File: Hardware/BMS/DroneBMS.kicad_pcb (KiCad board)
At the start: 4 copper layers, 90 x 51 mm, 42 parts, among them J1 BattLevel (ADC), J2 BattLevel (ADC), U1 LMR51430, U2 AMS1117-3.3

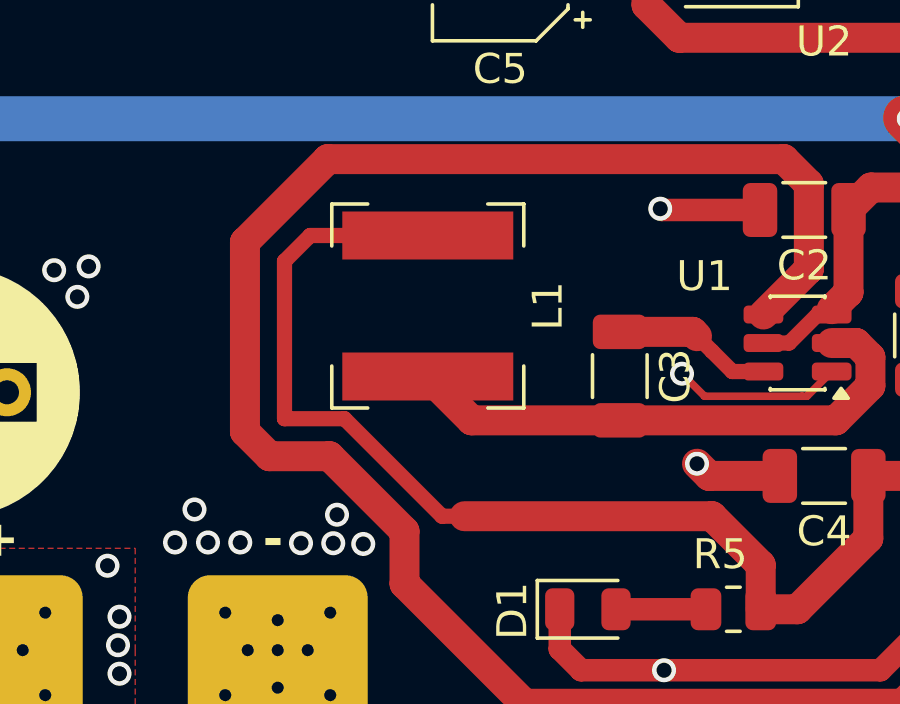
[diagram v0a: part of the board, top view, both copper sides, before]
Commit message: Updated Pcb Footprints
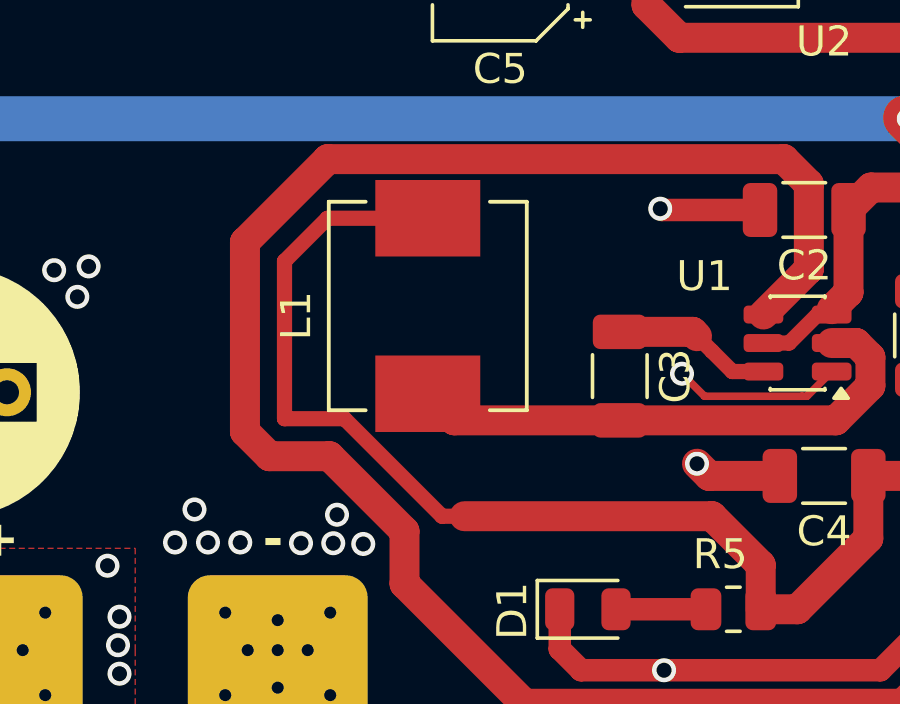
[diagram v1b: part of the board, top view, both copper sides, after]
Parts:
- L1: footprint Inductor_SMD:L_Bourns-SRN6028 -> Custom_Footprints:IND_VSAB0630-4R7M
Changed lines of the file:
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@@
 		)
 	)
-	(footprint "Inductor_SMD:L_Bourns-SRN6028"
+	(footprint "Custom_Footprints:IND_VSAB0630-4R7M"
 		(layer "F.Cu")
 		(at 160.5262 107.4928 90)
-		(descr "Bourns SRN6028 series SMD inductor")
-		(tags "Bourns SRN6028 SMD inductor")
 		(property "Reference" "L1"
-			(at 0 4 90)
+			(at -0.325 -4.385 90)
 			(layer "F.SilkS")
 			(effects
@@
 		)
 		(property "Value" "4.7uH"
-			(at 4.263 0.234 0)
+			(at 7.295 4.365 90)
 			(layer "F.Fab")
 			(effects
@@
 		(property "Datasheet" "~"
 			(at 0 0 90)
-			(unlocked yes)
 			(layer "F.Fab")
 			(hide yes)
@@
 		(property "Description" "Inductor"
 			(at 0 0 90)
-			(unlocked yes)
 			(layer "F.Fab")
 			(hide yes)
@@
 		(attr smd)
 		(fp_line
-			(start 3.4 -3.2)
-			(end 2 -3.2)
+			(start 3.475 -3.3)
+			(end 3.475 -2.07)
 			(stroke
-				(width 0.12)
+				(width 0.127)
 				(type solid)
 			)
@@
 		)
 		(fp_line
-			(start 3.4 -3.2)
-			(end 3.4 -2)
+			(start -3.475 -3.3)
+			(end 3.475 -3.3)
 			(stroke
-				(width 0.12)
+				(width 0.127)
 				(type solid)
 			)
@@
 		)
 		(fp_line
-			(start -3.4 -3.2)
-			(end -2 -3.2)
+			(start -3.475 -2.07)
+			(end -3.475 -3.3)
 			(stroke
-				(width 0.12)
+				(width 0.127)
 				(type solid)
 			)
@@
 		)
 		(fp_line
-			(start -3.4 -3.2)
-			(end -3.4 -2)
+			(start 3.475 2.07)
+			(end 3.475 3.3)
 			(stroke
-				(width 0.12)
+				(width 0.127)
 				(type solid)
 			)
@@
 		)
 		(fp_line
-			(start 3.4 3.2)
-			(end 3.4 2)
+			(start 3.475 3.3)
+			(end -3.475 3.3)
 			(stroke
-				(width 0.12)
+				(width 0.127)
 				(type solid)
 			)
@@
 		)
 		(fp_line
-			(start 3.4 3.2)
-			(end 2 3.2)
+			(start -3.475 3.3)
+			(end -3.475 2.07)
 			(stroke
-				(width 0.12)
+				(width 0.127)
 				(type solid)
 			)
@@
 		)
 		(fp_line
-			(start -3.4 3.2)
-			(end -3.4 2)
+			(start 3.725 -3.55)
+			(end 3.725 -2)
 			(stroke
-				(width 0.12)
+				(width 0.05)
 				(type solid)
 			)
-			(layer "F.SilkS")
+			(layer "F.CrtYd")
 		)
 		(fp_line
-			(start -3.4 3.2)
-			(end -2 3.2)
+			(start -3.725 -3.55)
+			(end 3.725 -3.55)
 			(stroke
-				(width 0.12)
+				(width 0.05)
 				(type solid)
 			)
-			(layer "F.SilkS")
+			(layer "F.CrtYd")
 		)
 		(fp_line
-			(start 3.3 -3.1)
-			(end 3.3 3.1)
+			(start 4.45 -2)
+			(end 4.45 2)
 			(stroke
 				(width 0.05)
@@
 		)
 		(fp_line
-			(start -3.3 -3.1)
-			(end 3.3 -3.1)
+			(start 3.725 -2)
+			(end 4.45 -2)
 			(stroke
 				(width 0.05)
@@
 		)
 		(fp_line
-			(start -3.3 -3.1)
-			(end -3.3 3.1)
+			(start -3.725 -2)
+			(end -3.725 -3.55)
 			(stroke
 				(width 0.05)
@@
 		)
 		(fp_line
-			(start 3.3 3.1)
-			(end -3.3 3.1)
+			(start -3.725 -2)
+			(end -4.45 -2)
 			(stroke
 				(width 0.05)
@@
 		)
 		(fp_line
-			(start 3.3 -3.1)
-			(end 3.3 3.1)
+			(start -4.45 -2)
+			(end -4.45 2)
 			(stroke
-				(width 0.1)
+				(width 0.05)
 				(type solid)
 			)
-			(layer "F.Fab")
+			(layer "F.CrtYd")
 		)
 		(fp_line
-			(start -3.3 -3.1)
-			(end 3.3 -3.1)
+			(start 4.45 2)
+			(end 3.725 2)
 			(stroke
-				(width 0.1)
+				(width 0.05)
 				(type solid)
 			)
-			(layer "F.Fab")
+			(layer "F.CrtYd")
 		)
 		(fp_line
-			(start -3.3 -3.1)
-			(end -3.3 3.1)
+			(start 3.725 2)
+			(end 3.725 3.55)
 			(stroke
-				(width 0.1)
+				(width 0.05)
+				(type solid)
+			)
+			(layer "F.CrtYd")
+		)
+		(fp_line
+			(start -4.45 2)
+			(end -3.725 2)
+			(stroke
+				(width 0.05)
+				(type solid)
+			)
+			(layer "F.CrtYd")
+		)
+		(fp_line
+			(start 3.725 3.55)
+			(end -3.725 3.55)
+			(stroke
+				(width 0.05)
+				(type solid)
+			)
+			(layer "F.CrtYd")
+		)
+		(fp_line
+			(start -3.725 3.55)
+			(end -3.725 2)
+			(stroke
+				(width 0.05)
+				(type solid)
+			)
+			(layer "F.CrtYd")
+		)
+		(fp_line
+			(start 3.475 -3.3)
+			(end 3.475 3.3)
+			(stroke
+				(width 0.127)
 				(type solid)
 			)
@@
 		)
 		(fp_line
-			(start 3.3 3.1)
-			(end -3.3 3.1)
+			(start -3.475 -3.3)
+			(end 3.475 -3.3)
 			(stroke
-				(width 0.1)
+				(width 0.127)
 				(type solid)
 			)
 			(layer "F.Fab")
 		)
-		(fp_text user "${REFERENCE}"
-			(at 0 0 90)
+		(fp_line
+			(start 3.475 3.3)
+			(end -3.475 3.3)
+			(stroke
+				(width 0.127)
+				(type solid)
+			)
 			(layer "F.Fab")
-			(effects
-				(font
-					(size 1 1)
-					(thickness 0.15)
-				)
+		)
+		(fp_line
+			(start -3.475 3.3)
+			(end -3.475 -3.3)
+			(stroke
+				(width 0.127)
+				(type solid)
 			)
+			(layer "F.Fab")
 		)
 		(pad "1" smd rect
-			(at -2.35 0 90)
-			(size 1.6 5.7)
+			(at -2.925 0 90)
+			(size 2.55 3.5)
 			(layers "F.Cu" "F.Mask" "F.Paste")
 			(net 4 "Net-(U1-SW)")
 			(pinfunction "1")
 			(pintype "passive")
+			(solder_mask_margin 0.102)
 		)
 		(pad "2" smd rect
-			(at 2.35 0 90)
-			(size 1.6 5.7)
+			(at 2.925 0 90)
+			(size 2.55 3.5)
 			(layers "F.Cu" "F.Mask" "F.Paste")
 			(net 3 "5V")
 			(pinfunction "2")
 			(pintype "passive")
+			(solder_mask_margin 0.102)
 		)
 		(embedded_fonts no)
-		(model "${KICAD9_3DMODEL_DIR}/Inductor_SMD.3dshapes/L_Bourns-SRN6028.step"
+		(model "C:/Users/Zahir/Downloads/VSAB0630-4R7M/VSAB0630-4R7M.step"
 			(offset
 				(xyz 0 0 0)
@@
 			)
 			(rotate
-				(xyz 0 0 0)
+				(xyz -90 -0 -0)
 			)
 		)
@@
 	)
 	(segment
-		(start 157.75 111.25)
-		(end 161 114.5)
-		(width 0.508)
-		(layer "F.Cu")
-		(net 3)
-	)
-	(segment
 		(start 179.959 110.109)
 		(end 177.5995 112.4685)
@@
 	(segment
 		(start 155.75 111.25)
-		(end 157.75 111.25)
+		(end 155.75 106)
 		(width 0.508)
 		(layer "F.Cu")
@@
 	)
 	(segment
+		(start 155.75 106)
+		(end 157.1822 104.5678)
+		(width 0.508)
+		(layer "F.Cu")
+		(net 3)
+	)
+	(segment
 		(start 178.943 98.552)
 		(end 168.91 98.552)
@@
 	)
 	(segment
+		(start 161.75 114.5)
+		(end 161 114.5)
+		(width 0.508)
+		(layer "F.Cu")
+		(net 3)
+	)
+	(segment
 		(start 181 100.609)
 		(end 178.943 98.552)
@@
 	)
 	(segment
+		(start 161 114.5)
+		(end 157.75 111.25)
+		(width 0.508)
+		(layer "F.Cu")
+		(net 3)
+	)
+	(segment
 		(start 181.864 111.06)
 		(end 186.4 115.596)
@@
 	)
 	(segment
-		(start 160.5262 105.1428)
-		(end 156.6072 105.1428)
-		(width 0.508)
-		(layer "F.Cu")
-		(net 3)
-	)
-	(segment
 		(start 164.755 96.407)
 		(end 164.741 96.393)
@@
 	)
 	(segment
-		(start 161 114.5)
-		(end 161.75 114.5)
-		(width 0.508)
-		(layer "F.Cu")
-		(net 3)
-	)
-	(segment
 		(start 168.91 98.552)
 		(end 167.817 97.459)
@@
 	)
 	(segment
+		(start 157.1822 104.5678)
+		(end 160.5262 104.5678)
+		(width 0.508)
+		(layer "F.Cu")
+		(net 3)
+	)
+	(segment
 		(start 171.624 117.602)
 		(end 172.847 117.602)
@@
 	)
 	(segment
-		(start 156.6072 105.1428)
-		(end 155.75 106)
-		(width 0.508)
+		(start 170 114.5)
+		(end 161.75 114.5)
+		(width 1)
 		(layer "F.Cu")
 		(net 3)
 	)
 	(segment
-		(start 170 114.5)
-		(end 161.75 114.5)
+		(start 181.864 110.109)
+		(end 179.959 110.109)
 		(width 1)
 		(layer "F.Cu")
@@
 	)
 	(segment
-		(start 155.75 106)
+		(start 157.75 111.25)
 		(end 155.75 111.25)
 		(width 0.508)
@@
 	)
 	(segment
-		(start 181.864 110.109)
-		(end 179.959 110.109)
+		(start 161.413 111.3046)
+		(end 160.5262 110.4178)
 		(width 1)
 		(layer "F.Cu")
-		(net 3)
+		(net 4)
 	)
 	(segment
-		(start 161.988 111.3046)
-		(end 160.5262 109.8428)
+		(start 166.927 111.3046)
+		(end 161.413 111.3046)
 		(width 1)
 		(layer "F.Cu")
@@
 	)
 	(segment
-		(start 161.5572 109.5756)
-		(end 161.544 109.5888)
-		(width 1)
-		(layer "F.Cu")
-		(net 4)
-	)
-	(segment
 		(start 174.129514 111.3046)
 		(end 166.927 111.3046)
 		(width 1)
 		(layer "F.Cu")
-		(net 4)
-	)
-	(segment
-		(start 166.927 111.3046)
-		(end 161.988 111.3046)
-		(width 1)
-		(layer "F.Cu")
